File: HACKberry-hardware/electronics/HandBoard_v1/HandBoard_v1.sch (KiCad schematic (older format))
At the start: 12 parts, among them CON1 BARREL_JACK_MJ179PH, SW1:MAX1 SW_PUSH_SKRGAQD010, SW2:MIN1 SW_PUSH_SKRGAQD010, SW3:Thumb1 SW_PUSH_SKRGAQD010, SW4:Middle1 SW_PUSH_SKRGAQD010, SW5 SWITCH_SS-12SDP2, U1 3-CONDUCTOR_MINIATUIRE_JACK_M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, U2 Arduino_Micro, U3 Seed_Studio_Adjustable_DC/DC_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, U4 Servo_Motor_S03N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

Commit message: Added garber data of SensorBoard
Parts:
- CON1: value BARREL_JACK_MJ179PH -> BARREL_JACK; footprint HACKberry_v1:MJ179PH -> (none)
- U1: value 3-CONDUCTOR_MINIATUIRE_JACK_MJ-4535-3 -> 3-CONDUCTOR_MINIATUIRE_JACK_MJ-4535-3-RESCUE-HandBoard_v1; footprint HACKberry_v1:MINIATURE_JACK_MJ-4535-3 -> (none)
- U2: footprint HACKberry_v1:Arduino_Micro -> (none)
- U3: footprint Pin_Headers:Pin_Header_Straight_2x02 -> (none)
- U4: footprint Pin_Headers:Pin_Header_Straight_1x03 -> (none)
- U5: value Servo_Motor_MG90S -> Servo_Motor_ASV15MG; footprint Pin_Headers:Pin_Header_Straight_1x03 -> (none)
- U6: value Servo_Motor_MG90S -> Servo_Motor_ASV15MB; footprint Pin_Headers:Pin_Header_Straight_1x03 -> (none)
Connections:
- net at U2.11 (11(PWM)): now also U1.2 (VCC)
- net at U2.3 (3(PWM)/SCL): now also SW2:MIN1.2; no longer U4.1 (INPUT)
- net at U2.3V3 (3.3V): no longer U1.2 (VCC)
- net at U2.5 (5(PWM)): now also SW4:Middle1.2; no longer U5.1 (INPUT)
- net at U2.6 (6(PWM)/A7): no longer U6.1 (INPUT)
- net at U2.8 (8/A8): now also U1.4 (INPUT)
- net at U2.A0: no longer U1.4 (INPUT)
- net at U2.A2: now also U6.1 (INPUT)
- net at U2.A3: now also U5.1 (INPUT); no longer SW4:Middle1.2
- net at U2.A4: now also SW1:MAX1.2; no longer SW3:Thumb1.2
- net at U2.A5: now also U4.1 (INPUT); no longer SW2:MIN1.2
- net at U2.A6 (4): now also SW3:Thumb1.2; no longer SW1:MAX1.2
- net at CON1.2, SW1:MAX1.1, SW2:MIN1.1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: now also U2.RX (0/RX); no longer U2.GND
- net at U2.TX (1/TX): now also SW5.1, U3.1 (IN+)
- now unconnected: U2.VIN
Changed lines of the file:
@@
 LIBS:valves
 LIBS:HandBoard_v1-cache
+LIBS:HACKberry_v1
 EELAYER 25 0
 EELAYER END
@@
 Comment4 ""
 $EndDescr
-$Comp
-L Arduino_Micro U2
-U 1 1 555EFCA5
-P 5500 4000
-F 0 "U2" H 5500 5000 60  0000 C CNN
-F 1 "Arduino_Micro" H 5500 3050 60  0000 C CNN
-F 2 "HACKberry_v1:Arduino_Micro" V 5500 4000 60  0001 C CNN
-F 3 "" V 5500 4000 60  0000 C CNN
-	1    5500 4000
-	-1   0    0    -1
-$EndComp
-$Comp
-L Servo_Motor U5
-U 1 1 555F1F15
-P 8050 4150
-F 0 "U5" H 7850 4450 60  0000 C CNN
-F 1 "Servo_Motor_MG90S" H 8050 4350 60  0000 C CNN
-F 2 "Pin_Headers:Pin_Header_Straight_1x03" H 8050 4350 60  0001 C CNN
-F 3 "" H 8050 4350 60  0000 C CNN
-	1    8050 4150
-	-1   0    0    -1
-$EndComp
-$Comp
-L Servo_Motor U4
-U 1 1 555F20CE
-P 8000 3650
-F 0 "U4" H 7800 3950 60  0000 C CNN
-F 1 "Servo_Motor_S03N" H 8000 3850 60  0000 C CNN
-F 2 "Pin_Headers:Pin_Header_Straight_1x03" H 8000 3850 60  0001 C CNN
-F 3 "" H 8000 3850 60  0000 C CNN
-	1    8000 3650
-	-1   0    0    -1
-$EndComp
-$Comp
-L Servo_Motor U6
-U 1 1 555F20F9
-P 8000 4650
-F 0 "U6" H 7800 4950 60  0000 C CNN
-F 1 "Servo_Motor_MG90S" H 8000 4850 60  0000 C CNN
-F 2 "Pin_Headers:Pin_Header_Straight_1x03" H 8000 4850 60  0001 C CNN
-F 3 "" H 8000 4850 60  0000 C CNN
-	1    8000 4650
-	-1   0    0    -1
-$EndComp
-$Comp
-L 3-CONDUCTOR_MINIATUIRE_JACK_MJ-4535-3-RESCUE-HandBoard_v1 U1
-U 1 1 555F3180
-P 3200 4700
-F 0 "U1" H 3000 5000 60  0000 C CNN
-F 1 "3-CONDUCTOR_MINIATUIRE_JACK_MJ-4535-3" H 3200 4900 60  0000 C CNN
-F 2 "HACKberry_v1:MINIATURE_JACK_MJ-4535-3" H 3200 4900 60  0001 C CNN
-F 3 "" H 3200 4900 60  0000 C CNN
-	1    3200 4700
-	1    0    0    -1
-$EndComp
 $Comp
 L SW_PUSH SW1:MAX1
@@
 	6800 4000 6800 3550
 Wire Wire Line
-	6800 3550 7650 3550
+	6800 3550 7700 3550
 Wire Wire Line
 	6250 4200 6800 4200
@@
 	6800 4300 6800 4550
 Wire Wire Line
-	6800 4550 7650 4550
+	6800 4550 7700 4550
 Wire Wire Line
 	3850 5000 3850 5500
 Wire Wire Line
-	3850 5500 5000 5500
-Wire Wire Line
-	7650 3650 6950 3650
+	3850 5500 5050 5500
+Wire Wire Line
+	7700 3650 6950 3650
 Wire Wire Line
 	6950 4150 7700 4150
 Wire Wire Line
-	6950 4650 7650 4650
+	6950 4650 7700 4650
 Connection ~ 6950 4150
 Wire Wire Line
 	6950 3650 6950 5300
 Wire Wire Line
-	6950 5300 6000 5300
+	6950 5300 6050 5300
 Connection ~ 6950 4650
 Wire Wire Line
@@
 	4350 3500 4350 5000
 Wire Wire Line
-	4350 4800 3550 4800
+	4350 4800 3500 4800
 Wire Wire Line
 	4350 5000 3850 5000
@@
 Connection ~ 2650 3800
 Wire Wire Line
-	7650 3750 7050 3750
+	7700 3750 7050 3750
 Wire Wire Line
 	7050 3750 7050 5500
 Wire Wire Line
-	7050 5500 6000 5500
+	7050 5500 6050 5500
 Wire Wire Line
 	7700 4250 7050 4250
 Connection ~ 7050 4250
 Wire Wire Line
-	7650 4750 7050 4750
+	7700 4750 7050 4750
 Connection ~ 7050 4750
 Wire Wire Line
@@
 	4900 4950 4900 5300
 Wire Wire Line
-	4900 5300 5000 5300
+	4900 5300 5050 5300
 Wire Wire Line
 	4650 4950 4900 4950
@@
 Wire Wire Line
 	4650 3400 4750 3400
-$Comp
-L BARREL_JACK CON1
-U 1 1 555F5A20
-P 3050 5200
-F 0 "CON1" H 3050 5450 60  0000 C CNN
-F 1 "BARREL_JACK_MJ179PH" H 3050 5000 60  0000 C CNN
-F 2 "HACKberry_v1:MJ179PH" H 3050 5200 60  0001 C CNN
-F 3 "" H 3050 5200 60  0000 C CNN
-	1    3050 5200
-	1    0    0    -1
-$EndComp
-Wire Wire Line
-	3350 5300 3850 5300
-Wire Wire Line
-	3350 5100 3550 5100
+Wire Wire Line
+	3300 5300 3850 5300
+Wire Wire Line
+	3300 5100 3550 5100
 Wire Wire Line
 	3550 5100 3550 5200
@@
 NoConn ~ 3350 5200
 Wire Wire Line
-	3550 4700 4750 4700
-Wire Wire Line
-	3550 4600 4550 4600
+	3500 4700 4750 4700
+Wire Wire Line
+	3500 4600 4550 4600
 Wire Wire Line
 	4550 4600 4550 4500
@@
 Wire Wire Line
 	3700 4200 4750 4200
-$Comp
-L Seed_Studio_Adjustable_DC/DC_Power_Converter_(1.25V_-_35V/3A) U3
-U 1 1 555F2DA3
-P 5500 5400
-F 0 "U3" H 5500 5650 60  0000 C CNN
-F 1 "Seed_Studio_Adjustable_DC/DC_Power_Converter_(1.25V_-_35V/3A)" H 5550 5150 60  0000 C CNN
-F 2 "Pin_Headers:Pin_Header_Straight_2x02" H 5550 5150 60  0001 C CNN
-F 3 "" H 5550 5150 60  0000 C CNN
-	1    5500 5400
-	1    0    0    -1
-$EndComp
 $Comp
 L SW_PUSH SW4:Middle1
@@
 	1    0    0    -1
 $EndComp
+$Comp
+L BARREL_JACK CON1
+U 1 1 55C49688
+P 3000 5200
+F 0 "CON1" H 3000 5450 60  0000 C CNN
+F 1 "BARREL_JACK" H 3000 5000 60  0000 C CNN
+F 2 "" H 3000 5200 60  0000 C CNN
+F 3 "" H 3000 5200 60  0000 C CNN
+	1    3000 5200
+	1    0    0    -1
+$EndComp
+$Comp
+L Seed_Studio_Adjustable_DC/DC_Power_Converter_(1.25V_-_35V/3A) U3
+U 1 1 55C499A9
+P 5550 5400
+F 0 "U3" H 5550 5650 60  0000 C CNN
+F 1 "Seed_Studio_Adjustable_DC/DC_Power_Converter_(1.25V_-_35V/3A)" H 5600 5150 60  0000 C CNN
+F 2 "" H 5600 5150 60  0000 C CNN
+F 3 "" H 5600 5150 60  0000 C CNN
+	1    5550 5400
+	1    0    0    -1
+$EndComp
+$Comp
+L Arduino_Micro U2
+U 1 1 55C4A094
+P 5500 4000
+F 0 "U2" H 5500 5000 60  0000 C CNN
+F 1 "Arduino_Micro" H 5500 3000 60  0000 C CNN
+F 2 "" H 5500 5000 60  0000 C CNN
+F 3 "" H 5500 5000 60  0000 C CNN
+	1    5500 4000
+	1    0    0    -1
+$EndComp
+$Comp
+L Servo_Motor U4
+U 1 1 55C4A9EF
+P 8050 3650
+F 0 "U4" H 7850 3950 60  0000 C CNN
+F 1 "Servo_Motor_S03N" H 8050 3850 60  0000 C CNN
+F 2 "" H 8050 3850 60  0000 C CNN
+F 3 "" H 8050 3850 60  0000 C CNN
+	1    8050 3650
+	-1   0    0    -1
+$EndComp
+$Comp
+L Servo_Motor U5
+U 1 1 55C4ACAA
+P 8050 4150
+F 0 "U5" H 7850 4450 60  0000 C CNN
+F 1 "Servo_Motor_ASV15MG" H 8050 4350 60  0000 C CNN
+F 2 "" H 8050 4350 60  0000 C CNN
+F 3 "" H 8050 4350 60  0000 C CNN
+	1    8050 4150
+	-1   0    0    -1
+$EndComp
+$Comp
+L Servo_Motor U6
+U 1 1 55C4ACE8
+P 8050 4650
+F 0 "U6" H 7850 4950 60  0000 C CNN
+F 1 "Servo_Motor_ASV15MB" H 8050 4850 60  0000 C CNN
+F 2 "" H 8050 4850 60  0000 C CNN
+F 3 "" H 8050 4850 60  0000 C CNN
+	1    8050 4650
+	-1   0    0    -1
+$EndComp
+$Comp
+L 3-CONDUCTOR_MINIATUIRE_JACK_MJ-4535-3-RESCUE-HandBoard_v1 U1
+U 1 1 55C4B2D6
+P 3150 4700
+F 0 "U1" H 2950 5000 60  0000 C CNN
+F 1 "3-CONDUCTOR_MINIATUIRE_JACK_MJ-4535-3-RESCUE-HandBoard_v1" H 3150 4900 60  0000 C CNN
+F 2 "" H 3150 4900 60  0000 C CNN
+F 3 "" H 3150 4900 60  0000 C CNN
+	1    3150 4700
+	1    0    0    -1
+$EndComp

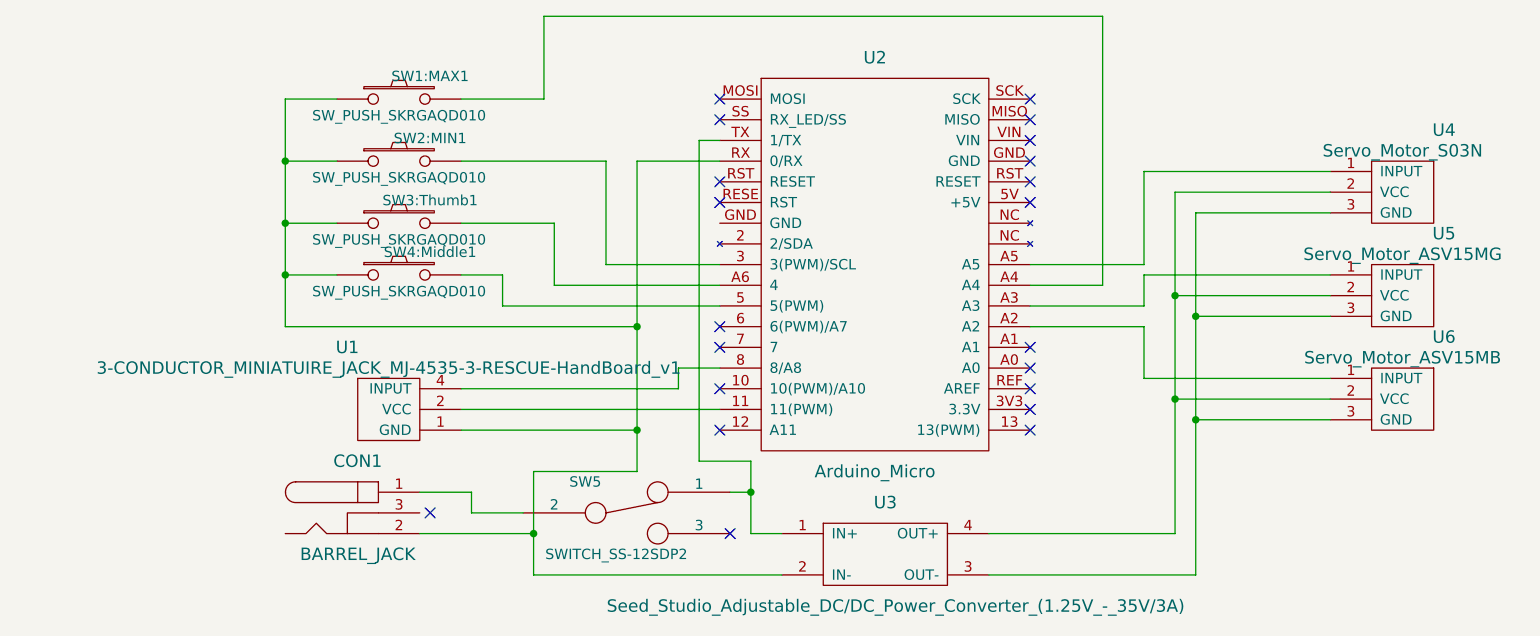
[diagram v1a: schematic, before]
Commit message: Changed the small servo and fixed minor errors.
Changed ASV-15MG to ES08MD.
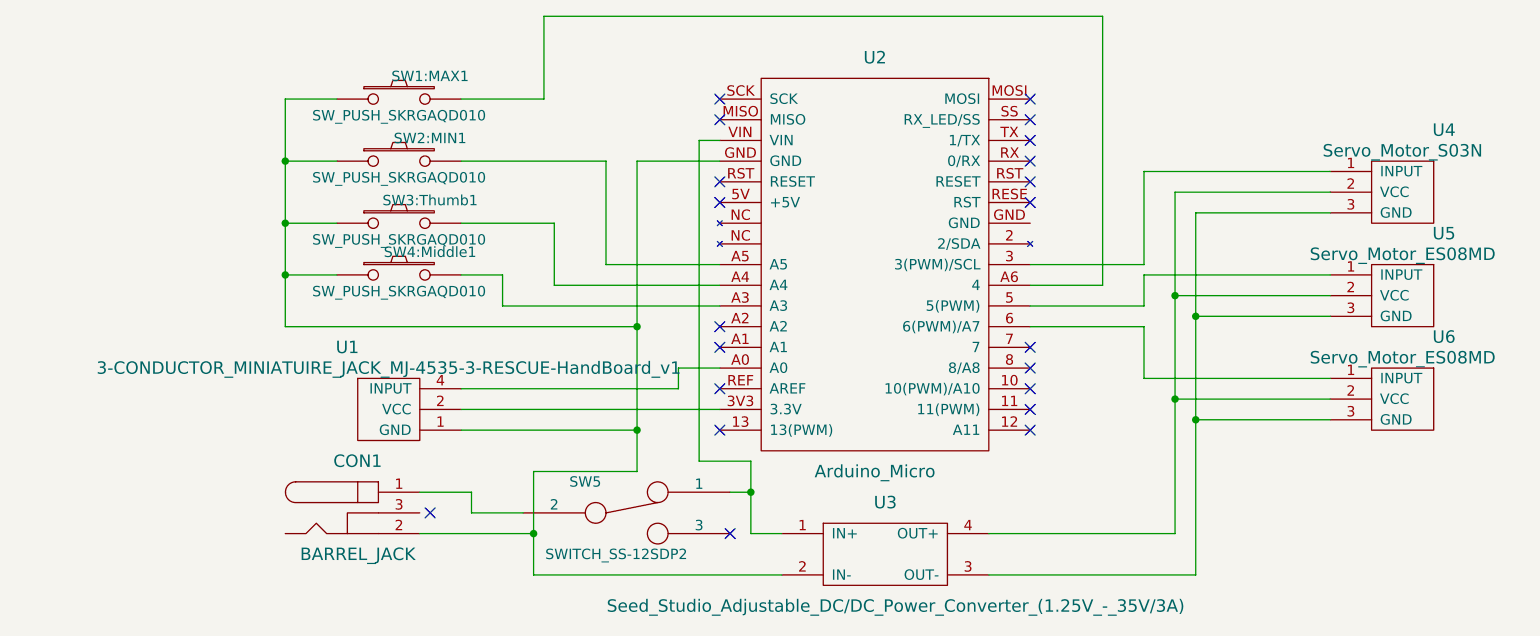
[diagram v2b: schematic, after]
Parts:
- U5: value Servo_Motor_ASV15MG -> Servo_Motor_ES08MD
- U6: value Servo_Motor_ASV15MB -> Servo_Motor_ES08MD
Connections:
- net at CON1.2, SW1:MAX1.1, SW2:MIN1.1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: now also U2.GND; no longer U2.RX (0/RX)
- net at SW1:MAX1.2: now also U2.A6 (4); no longer U2.A4
- net at SW2:MIN1.2: now also U2.A5; no longer U2.3 (3(PWM)/SCL)
- net at SW3:Thumb1.2: now also U2.A4; no longer U2.A6 (4)
- net at SW5.1, U3.1 (IN+): now also U2.VIN; no longer U2.TX (1/TX)
- net at SW4:Middle1.2: now also U2.A3; no longer U2.5 (5(PWM))
- net at U2.11 (11(PWM)): no longer U1.2 (VCC)
- net at U2.3V3 (3.3V): now also U1.2 (VCC)
- net at U2.6 (6(PWM)/A7): now also U6.1 (INPUT)
- net at U2.8 (8/A8): no longer U1.4 (INPUT)
- net at U2.A0: now also U1.4 (INPUT)
- net at U2.A2: no longer U6.1 (INPUT)
- net at U5.1 (INPUT): now also U2.5 (5(PWM)); no longer U2.A3
- net at U4.1 (INPUT): now also U2.3 (3(PWM)/SCL); no longer U2.A5
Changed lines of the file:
@@
 F 3 "" H 5500 5000 60  0000 C CNN
 	1    5500 4000
-	1    0    0    -1
+	-1   0    0    -1
 $EndComp
 $Comp
@@
 P 8050 4150
 F 0 "U5" H 7850 4450 60  0000 C CNN
-F 1 "Servo_Motor_ASV15MG" H 8050 4350 60  0000 C CNN
+F 1 "Servo_Motor_ES08MD" H 8050 4350 60  0000 C CNN
 F 2 "" H 8050 4350 60  0000 C CNN
 F 3 "" H 8050 4350 60  0000 C CNN
@@
 P 8050 4650
 F 0 "U6" H 7850 4950 60  0000 C CNN
-F 1 "Servo_Motor_ASV15MB" H 8050 4850 60  0000 C CNN
+F 1 "Servo_Motor_ES08MD" H 8050 4850 60  0000 C CNN
 F 2 "" H 8050 4850 60  0000 C CNN
 F 3 "" H 8050 4850 60  0000 C CNN

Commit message: Change DC-jack to PJ-102A
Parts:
- CON1: footprint (none) -> HACKberry_v1:PJ-102A
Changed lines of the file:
@@
 F 0 "CON1" H 3000 5450 60  0000 C CNN
 F 1 "BARREL_JACK" H 3000 5000 60  0000 C CNN
-F 2 "" H 3000 5200 60  0000 C CNN
+F 2 "HACKberry_v1:PJ-102A" H 3000 5200 60  0001 C CNN
 F 3 "" H 3000 5200 60  0000 C CNN
 	1    3000 5200
@@
 F 0 "U3" H 5550 5650 60  0000 C CNN
 F 1 "Seed_Studio_Adjustable_DC/DC_Power_Converter_(1.25V_-_35V/3A)" H 5600 5150 60  0000 C CNN
-F 2 "" H 5600 5150 60  0000 C CNN
+F 2 "" H 5600 5150 60  0001 C CNN
 F 3 "" H 5600 5150 60  0000 C CNN
 	1    5550 5400
@@
 F 0 "U2" H 5500 5000 60  0000 C CNN
 F 1 "Arduino_Micro" H 5500 3000 60  0000 C CNN
-F 2 "" H 5500 5000 60  0000 C CNN
+F 2 "" H 5500 5000 60  0001 C CNN
 F 3 "" H 5500 5000 60  0000 C CNN
 	1    5500 4000
@@
 F 0 "U4" H 7850 3950 60  0000 C CNN
 F 1 "Servo_Motor_S03N" H 8050 3850 60  0000 C CNN
-F 2 "" H 8050 3850 60  0000 C CNN
+F 2 "" H 8050 3850 60  0001 C CNN
 F 3 "" H 8050 3850 60  0000 C CNN
 	1    8050 3650
@@
 F 0 "U5" H 7850 4450 60  0000 C CNN
 F 1 "Servo_Motor_ES08MD" H 8050 4350 60  0000 C CNN
-F 2 "" H 8050 4350 60  0000 C CNN
+F 2 "" H 8050 4350 60  0001 C CNN
 F 3 "" H 8050 4350 60  0000 C CNN
 	1    8050 4150
@@
 F 0 "U6" H 7850 4950 60  0000 C CNN
 F 1 "Servo_Motor_ES08MD" H 8050 4850 60  0000 C CNN
-F 2 "" H 8050 4850 60  0000 C CNN
+F 2 "" H 8050 4850 60  0001 C CNN
 F 3 "" H 8050 4850 60  0000 C CNN
 	1    8050 4650
@@
 F 0 "U1" H 2950 5000 60  0000 C CNN
 F 1 "3-CONDUCTOR_MINIATUIRE_JACK_MJ-4535-3-RESCUE-HandBoard_v1" H 3150 4900 60  0000 C CNN
-F 2 "" H 3150 4900 60  0000 C CNN
+F 2 "" H 3150 4900 60  0001 C CNN
 F 3 "" H 3150 4900 60  0000 C CNN
 	1    3150 4700
